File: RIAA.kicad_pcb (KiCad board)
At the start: 2 copper layers, 112 x 202 mm, 61 parts, among them K1 G6K-2, P10 From Keyboard, P8 From main PCB, P9 From Wire, Q1 BCV49, U5 OPA2134, U6 OPA2134, U7 LM317_TO-220

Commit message: Ceramic capacitors, 38 dB gain, output resistors and 4004 checks
- C1, C34/C35 and C107/C207 are now 1206 ceramics (C34/C35 22 uF to
  allow for DC-bias loss); the six remaining electrolytics are where a
  ceramic would be microphonic or add distortion (see design notes).
- R109/R209 4.3k -> 7.5k (RESI PTFR1206B7K50P9, C351451): gain about
  38 dB, to suit B&O's low-output MMC cartridges.
- New R113/R213 (100 R, C17901) between each op-amp output and its
  output capacitor, outside the feedback loop.
- P9 pins 2/4 are no-connects, matching the original P9 pin layout, so
  a 4004 harness no longer shorts the Beomaster 2400 remote lines; a
  ground via keeps K1's mute contact on the plane.
- Checked against the BeoGram 4004 service manual: P10 power pins match
  the 4004 module (8005022); its remote circuit is not supported.
- U7 value "LM317", 0.15 mm stroke on the section labels, datasheet
  fields synced, teardrops and zones rebuilt; ERC/DRC clean.
- README, design notes, changelog, render and response chart updated.

Co-Authored-By: Claude Opus 5.5 <noreply@anthropic.com>
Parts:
- added R113: 100, Resistor_SMD:R_1206_3216Metric_Pad1.30x1.75mm_HandSolder, F.Cu at (225.3, 121.3)
- added R213: 100, Resistor_SMD:R_1206_3216Metric_Pad1.30x1.75mm_HandSolder, F.Cu at (224.8, 91.8)
- C1: value 470uF -> 10uF; footprint Capacitor_SMD:CP_Elec_10x10.5 -> Capacitor_SMD:C_1206_3216Metric_Pad1.33x1.80mm_HandSolder
- C107, C207: footprint Capacitor_SMD:CP_Elec_5x5.4 -> Capacitor_SMD:C_1206_3216Metric_Pad1.33x1.80mm_HandSolder
- C34, C35: value 10uF -> 22uF; footprint Capacitor_SMD:CP_Elec_5x5.4 -> Capacitor_SMD:C_1206_3216Metric_Pad1.33x1.80mm_HandSolder
- R109, R209: value 4.3k -> 7.5k
- U7: value LM317_TO-220 -> LM317
- moved C1 13.8 mm to (183.9, 110.8), turned to 90 degrees
- moved NT1 6.82 mm to (209.0, 127.2), turned to -90 degrees
- moved R24 2.90 mm to (200.1, 132.6), turned to 180 degrees
- moved NT2 2.19 mm to (209.4, 97.2)
- moved C34 1.87 mm to (204.5, 136.8)
- moved C35 1.09 mm to (201.3, 98.6), turned to 180 degrees
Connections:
- P9 pad 2: GND -> unconnected-(P9-Pin_2-Pad2)
- P9 pad 4: GND -> unconnected-(P9-Pin_4-Pad4)
- R109 pad 1: Net-(C107-Pad1) -> Net-(R109-Pad1)
- R209 pad 1: Net-(C207-Pad1) -> Net-(R209-Pad1)
- U5 pad 7: Net-(C107-Pad1) -> Net-(R109-Pad1)
- U6 pad 7: Net-(C207-Pad1) -> Net-(R209-Pad1)
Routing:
- net Net-(C207-Pad1): track 30.1 -> 2.97 mm
- net Net-(C107-Pad1): track 30.1 -> 3.11 mm
- net Net-(R209-Pad1): track 0.00 -> 26.1 mm
- net Net-(R109-Pad1): track 0.00 -> 25.7 mm
- net 24VDC+: track 210.5 -> 197.3 mm
- net GND L IN PICKUP: track 81.9 -> 72.6 mm
- net Net-(U5B-+): track 51.9 -> 49.1 mm
- net Net-(U6B-+): track 53.0 -> 50.9 mm
- net VREF_R: track 26.3 -> 24.4 mm, vias 0 -> 2
- net Net-(U5A-+): track 19.4 -> 18.0 mm
- net Net-(U6A-+): track 19.9 -> 18.7 mm
- net VREF_L: track 27.8 -> 26.6 mm
- net RELAY ON: track 47.2 -> 46.2 mm
- net R OUT: track 52.2 -> 51.7 mm
- net GND: vias 2 -> 3

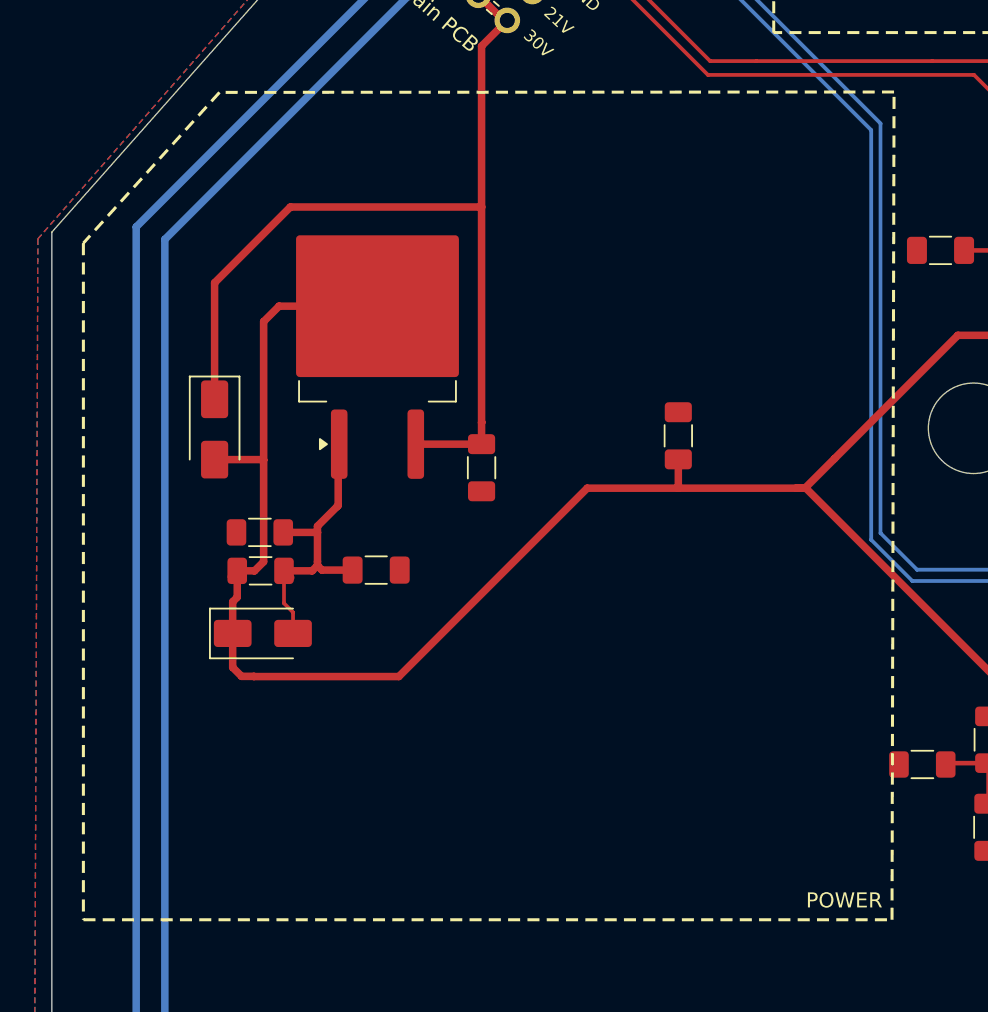
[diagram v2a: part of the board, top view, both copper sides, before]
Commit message: Schematic tidy-up: ERC without warnings, relay part named
- D5-D8 use the plain diode symbol (were drawn as Zeners; same pins).
- Duplicate net names removed: GND MB and GND CHASSIS labels are now
  GND, L/R OUT RIAA are now L/R OUT. Connectivity is unchanged
  (netlist compared before and after).
- RV1's embedded symbol matches the library.
- K1 value reads G6K-2F-Y DC24, the 24 V part already on the BOM.
- POWER silkscreen outline and label moved 0.7 mm left, off R24's pad.
- Design notes: relay contacts described correctly (commons 3/6 on GND,
  normally-closed 2/7 on the outputs); README names the 24 V relay.

ERC: 0 errors, 0 warnings. DRC: 0 errors, 0 unconnected, 0 parity
issues; the only notes are P8/P9/P10 having teardrops on their pads.

Co-Authored-By: Claude Opus 5.5 <noreply@anthropic.com>
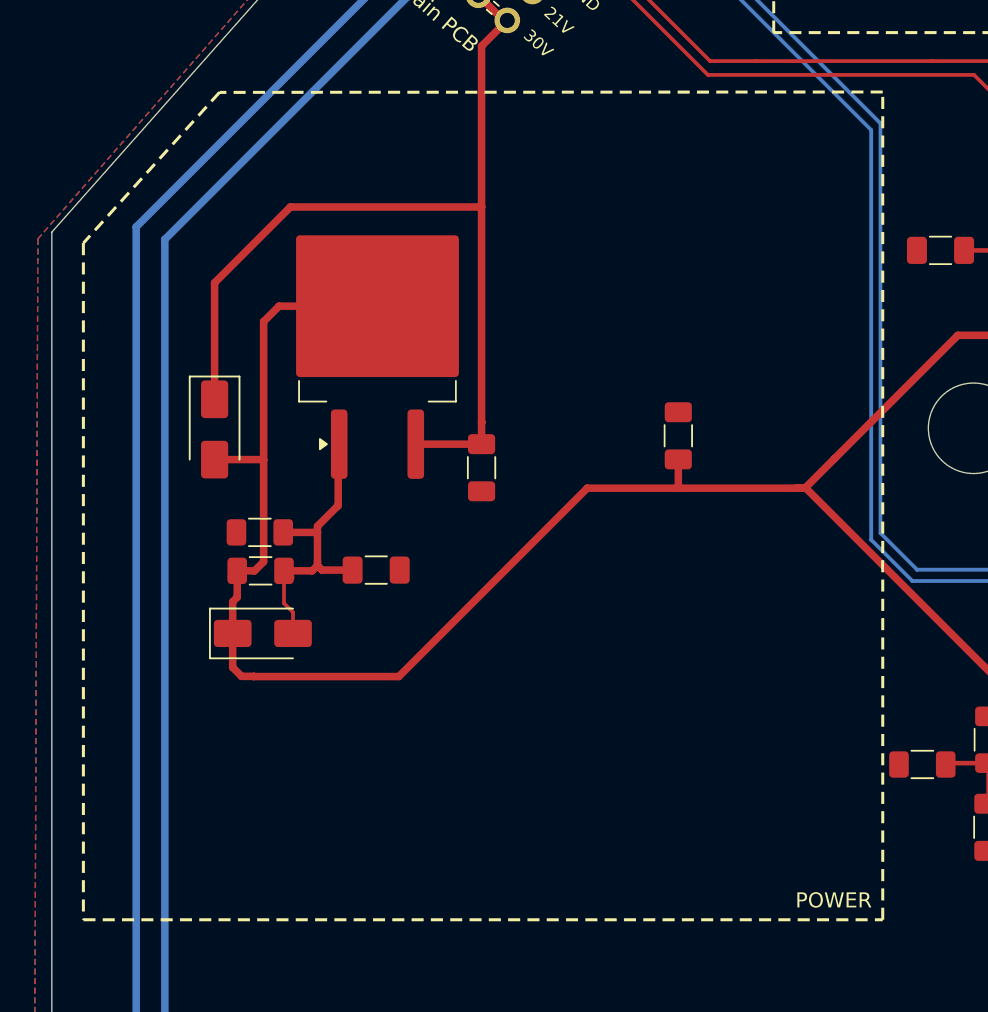
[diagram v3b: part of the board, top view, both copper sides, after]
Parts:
- K1: value G6K-2 -> G6K-2F-Y DC24
